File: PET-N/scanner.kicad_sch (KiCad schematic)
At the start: 14 parts, among them J4 AVR-ISP-6, U2 ATmega32A-A, U3 74HCT85, U4 74LS174, U6 74LS174, U7 74LS145, Y1 ASE-xxxMHz

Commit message: almost done routing; last checks still open
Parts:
- added C30: 100n, Capacitor_SMD:C_0805_2012Metric_Pad1.18x1.45mm_HandSolder, symbol Device:C
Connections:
- net GND: now also C30.1
- net VCC: now also C30.2
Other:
- note added: "(C) 2020,2021 Steve J. Gray (C) 2025 André Fachat"
- note added: "CBM-KEYB-PETN-3.0-20251005"
- note added: "This AtMega translates keyboard maps - S0-S1 inputs are on port bits PB0-3, on a port not written to. Reason is they can be read and converted into a table index using ANDI #15 - PB4 could in theory be used to extend the keyboard mapping table - PD2 is falling edge triggered interrupt, fed from the comparison between the S0-3 inputs and their delayed version. - U6 and U4 delay by at least two syt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"
- note removed: "This AtMega translates keyboard maps - S0-S1 inputs are on port bits PB0-3, on a port not written to. Reason is they can be read and converted into a table index using ANDI #15 - PB4 could in theory be used to extend the keyboard mapping table, as fed from PD3. - PD2 is falling edge triggered interrupt, fed from the comparison between the S0-3 inputs and their delayed version. - U6 and U4 delay b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"
- moved on the sheet: C12
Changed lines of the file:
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@@
 	(generator_version "9.0")
 	(paper "A4")
-	(text "This AtMega translates keyboard maps\n- S0-S1 inputs are on port bits PB0-3, on a port\n  not written to. Reason is they can be read and\n  converted into a table index using ANDI #15\n- PB4 could in theory be used to extend the keyboard\n  mapping table, as fed from PD3.\n- PD2 is falling edge triggered interrupt, fed from the\n  comparison between the S0-3 inputs and their delayed\n  version. \n- U6 and U4 delay by at least two sytem clocks cycles, to \n  ensure an interrupt is detected."
+	(text "CBM-KEYB-PETN-3.0-20251005"
 		(exclude_from_sim no)
-		(at 20.574 176.911 0)
+		(at 231.14 172.212 0)
 		(effects
 			(font
-				(size 2 2)
+				(size 4 4)
+				(thickness 0.9)
+				(bold yes)
+			)
+		)
+	)
+	(text "This AtMega translates keyboard maps\n- S0-S1 inputs are on port bits PB0-3, on a port\n  not written to. Reason is they can be read and\n  converted into a table index using ANDI #15\n- PB4 could in theory be used to extend the keyboard\n  mapping table\n- PD2 is falling edge triggered interrupt, fed from the\n  comparison between the S0-3 inputs and their delayed\n  version. \n- U6 and U4 delay by at least two sytem clocks cycles, to \n  ensure an interrupt is detected."
+		(exclude_from_sim no)
+		(at 22.352 173.736 0)
+		(effects
+			(font
+				(size 2.3 2.3)
 			)
 			(justify left)
 		)
 	)
+	(text "(C) 2020,2021 Steve J. Gray\n(C) 2025 André Fachat"
+		(exclude_from_sim no)
+		(at 249.936 181.102 0)
+		(effects
+			(font
+				(size 2.54 2.54)
+				(thickness 0.508)
+				(bold yes)
+			)
+		)
+	)
 	(junction
 		(at 259.08 23.495)
@@
 	)
 	(junction
+		(at 269.875 23.495)
+		(diameter 0)
+		(color 0 0 0 0)
+	)
+	(junction
 		(at 156.21 20.955)
 		(diameter 0)
@@
 	)
 	(junction
+		(at 269.875 36.195)
+		(diameter 0)
+		(color 0 0 0 0)
+	)
+	(junction
 		(at 43.18 26.035)
 		(diameter 0)
@@
 	(wire
 		(pts
-			(xy 270.51 36.195) (xy 259.08 36.195)
-		)
-		(stroke
-			(width 0)
-			(type default)
-		)
-	)
-	(wire
-		(pts
 			(xy 234.95 23.495) (xy 234.95 26.035)
 		)
@@
 	(wire
 		(pts
-			(xy 259.08 23.495) (xy 270.51 23.495)
+			(xy 259.08 23.495) (xy 269.875 23.495)
 		)
 		(stroke
@@
 	(wire
 		(pts
+			(xy 280.67 44.45) (xy 280.67 23.495)
+		)
+		(stroke
+			(width 0)
+			(type default)
+		)
+	)
+	(wire
+		(pts
 			(xy 151.13 125.095) (xy 140.97 125.095)
 		)
@@
 	(wire
 		(pts
+			(xy 269.875 23.495) (xy 280.67 23.495)
+		)
+		(stroke
+			(width 0)
+			(type default)
+		)
+	)
+	(wire
+		(pts
 			(xy 31.75 130.175) (xy 31.75 135.255)
 		)
@@
 	(wire
 		(pts
+			(xy 269.875 44.45) (xy 271.145 44.45)
+		)
+		(stroke
+			(width 0)
+			(type default)
+		)
+	)
+	(wire
+		(pts
 			(xy 247.65 36.195) (xy 234.95 36.195)
 		)
@@
 	(wire
 		(pts
-			(xy 270.51 26.035) (xy 270.51 23.495)
+			(xy 269.875 26.035) (xy 269.875 23.495)
 		)
 		(stroke
@@
 	(wire
 		(pts
+			(xy 269.875 36.195) (xy 259.08 36.195)
+		)
+		(stroke
+			(width 0)
+			(type default)
+		)
+	)
+	(wire
+		(pts
 			(xy 248.92 45.085) (xy 246.38 45.085)
 		)
@@
 	(wire
 		(pts
-			(xy 270.51 33.655) (xy 270.51 36.195)
+			(xy 269.875 33.655) (xy 269.875 36.195)
 		)
 		(stroke
@@
 	(wire
 		(pts
+			(xy 278.765 44.45) (xy 280.67 44.45)
+		)
+		(stroke
+			(width 0)
+			(type default)
+		)
+	)
+	(wire
+		(pts
 			(xy 44.45 23.495) (xy 154.94 23.495)
 		)
@@
 	(wire
 		(pts
+			(xy 269.875 36.195) (xy 269.875 44.45)
+		)
+		(stroke
+			(width 0)
+			(type default)
+		)
+	)
+	(wire
+		(pts
 			(xy 234.95 33.655) (xy 234.95 36.195)
 		)
@@
 	(symbol
 		(lib_id "Device:C")
-		(at 270.51 29.845 0)
+		(at 269.875 29.845 0)
 		(unit 1)
 		(exclude_from_sim no)
@@
 		(fields_autoplaced yes)
 		(property "Reference" "C12"
-			(at 274.32 28.5749 0)
+			(at 273.685 28.5749 0)
 			(effects
 				(font
@@
 		)
 		(property "Value" "100n"
-			(at 274.32 31.1149 0)
+			(at 273.685 31.1149 0)
 			(effects
 				(font
@@
 		)
 		(property "Footprint" "Capacitor_SMD:C_0805_2012Metric_Pad1.18x1.45mm_HandSolder"
-			(at 271.4752 33.655 0)
+			(at 270.8402 33.655 0)
 			(effects
 				(font
@@
 		)
 		(property "Datasheet" "~"
-			(at 270.51 29.845 0)
+			(at 269.875 29.845 0)
 			(effects
 				(font
@@
 		)
 		(property "Description" "Unpolarized capacitor"
-			(at 270.51 29.845 0)
+			(at 269.875 29.845 0)
 			(effects
 				(font
@@
 		)
 		(property "LCSC" "C14663"
-			(at 274.32 28.5749 0)
+			(at 273.685 28.5749 0)
 			(effects
 				(font
@@
 					(unit 1)
 				)
+			)
+		)
+	)
+	(symbol
+		(lib_id "Device:C")
+		(at 274.955 44.45 90)
+		(unit 1)
+		(exclude_from_sim no)
+		(in_bom yes)
+		(on_board yes)
+		(dnp no)
+		(fields_autoplaced yes)
+		(property "Reference" "C30"
+			(at 274.955 36.83 90)
+			(effects
+				(font
+					(size 1.27 1.27)
+				)
+			)
+		)
+		(property "Value" "100n"
+			(at 274.955 39.37 90)
+			(effects
+				(font
+					(size 1.27 1.27)
+				)
+			)
+		)
+		(property "Footprint" "Capacitor_SMD:C_0805_2012Metric_Pad1.18x1.45mm_HandSolder"
+			(at 278.765 43.4848 0)
+			(effects
+				(font
+					(size 1.27 1.27)
+				)
+				(hide yes)
+			)
+		)
+		(property "Datasheet" "~"
+			(at 274.955 44.45 0)
+			(effects
+				(font
+					(size 1.27 1.27)
+				)
+				(hide yes)
+			)
+		)
+		(property "Description" "Unpolarized capacitor"
+			(at 274.955 44.45 0)
+			(effects
+				(font
+					(size 1.27 1.27)
+				)
+				(hide yes)
+			)
+		)
+		(property "LCSC" "C14663"
+			(at 273.6849 40.64 0)
+			(effects
+				(font
+					(size 1.27 1.27)
+				)
+				(hide yes)
+			)
+		)
+		(pin "2"
+		)
+		(pin "1"
+		)
+		(instances
+			(project "petkn"
+				(path "/a0727808-af70-4056-b2ee-ab828c2acfbd/517ec251-9cce-431a-9802-232702808e0f"
+					(reference "C30")
+					(unit 1)
+				)

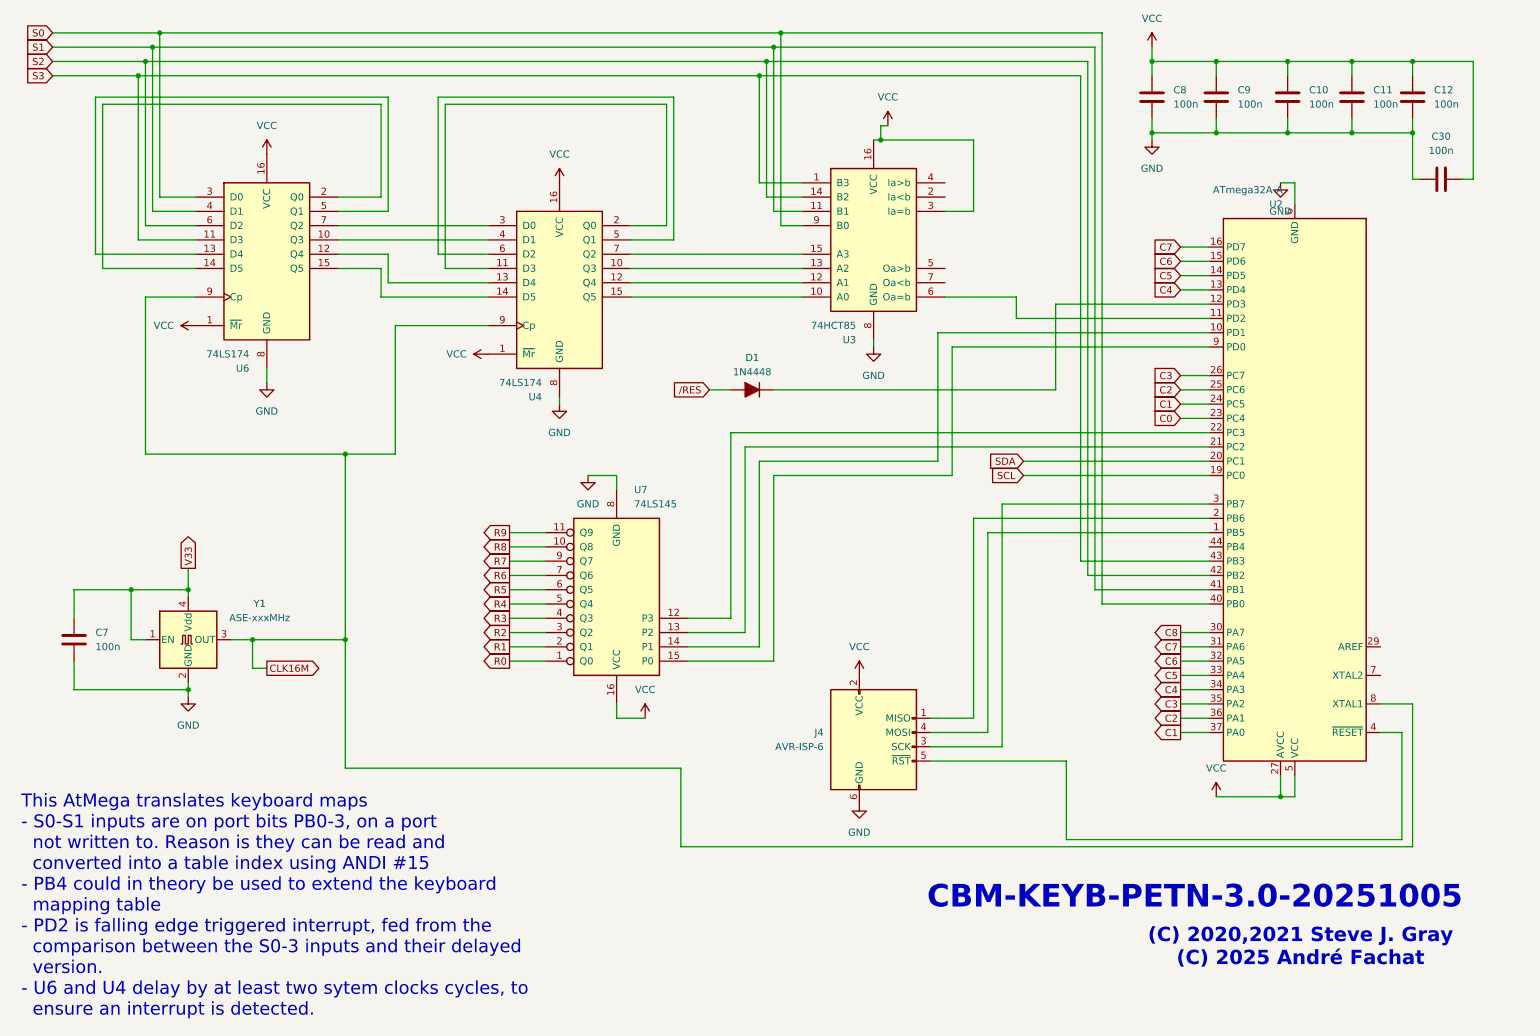
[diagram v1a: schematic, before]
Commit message: fix Cn vs CCn bug, add proper joystick in schem; routing still to fix
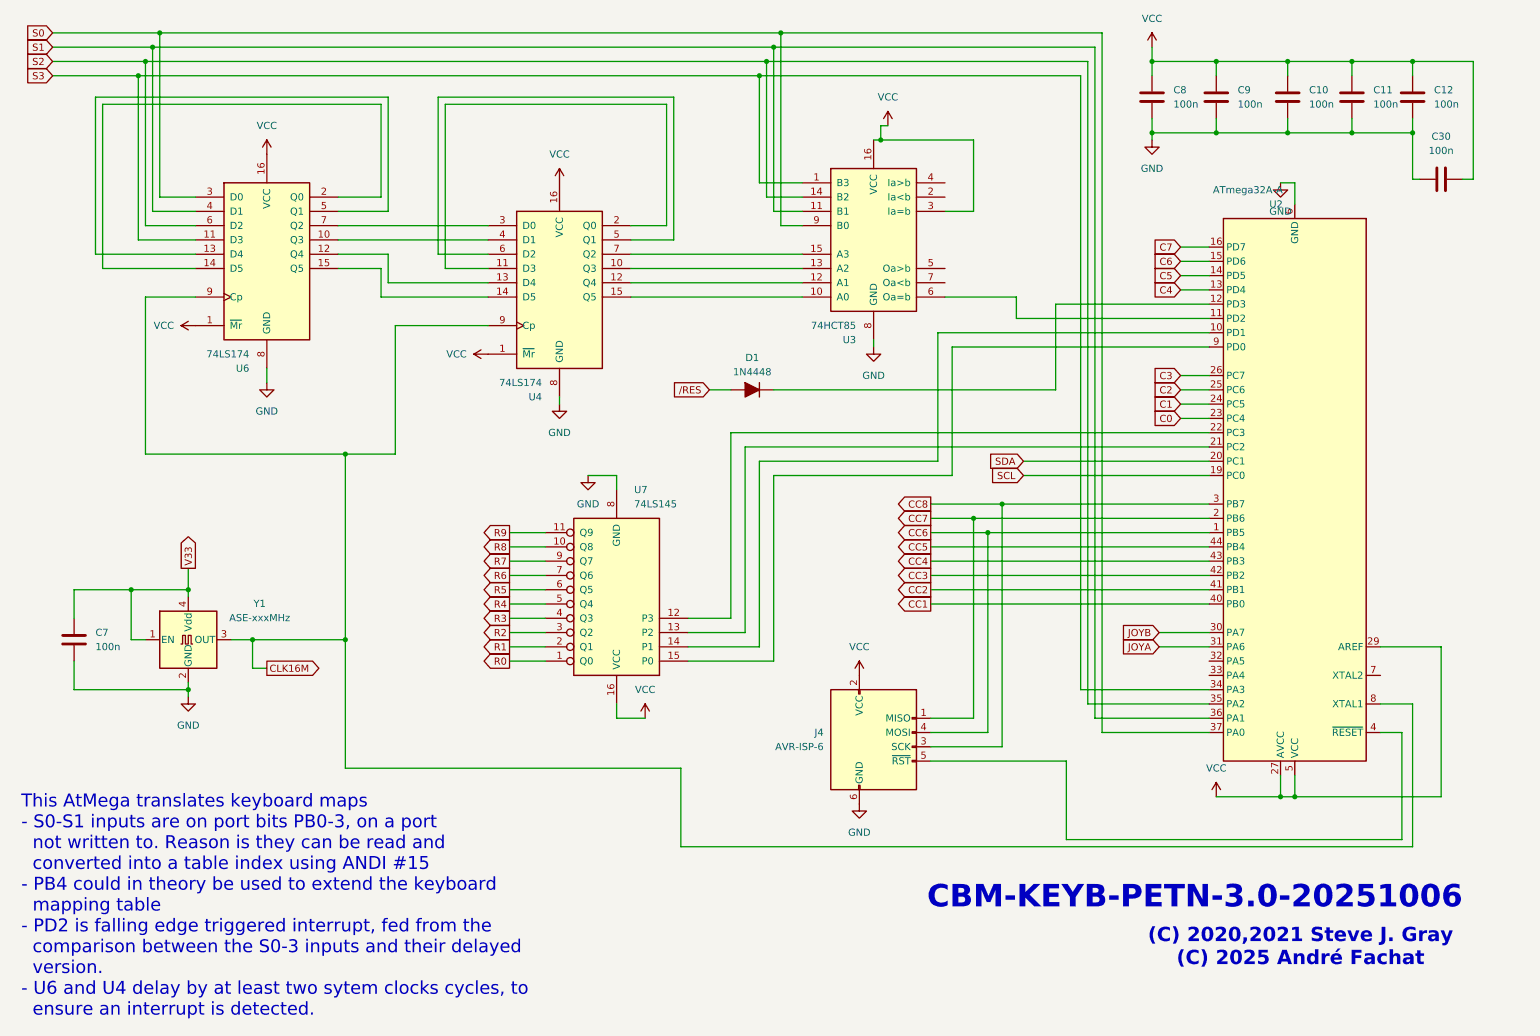
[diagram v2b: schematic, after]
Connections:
- net C1: no longer U2.37 (PA0)
- net C2: no longer U2.36 (PA1)
- net C3: no longer U2.35 (PA2)
- net C4: no longer U2.34 (PA3)
- net C5: no longer U2.33 (PA4)
- net C6: no longer U2.32 (PA5)
- net C7: no longer U2.31 (PA6)
- net S0: now also U2.37 (PA0); no longer U2.40 (PB0)
- net S1: now also U2.36 (PA1); no longer U2.41 (PB1)
- net S2: now also U2.35 (PA2); no longer U2.42 (PB2)
- net S3: now also U2.34 (PA3); no longer U2.43 (PB3)
- net VCC: now also U2.29 (AREF)
- net CC7: now reaches J4.1 (MISO), U2.2 (PB6)
- net CC8: now reaches J4.3 (SCK), U2.3 (PB7)
- net CC6: now reaches J4.4 (MOSI), U2.1 (PB5)
- net CC5: now reaches U2.44 (PB4)
- net C8 renamed JOYB
- new net CC1: U2.40 (PB0)
- new net CC2: U2.41 (PB1)
- new net CC3: U2.42 (PB2)
- new net CC4: U2.43 (PB3)
- new net JOYA: U2.31 (PA6)
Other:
- note added: "CBM-KEYB-PETN-3.0-20251006"
- note removed: "CBM-KEYB-PETN-3.0-20251005"

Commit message: hopefully final schem and layout for 3.0A
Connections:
- net C0 is gone; now on net C1: U2.23 (PC4)
- net C1: no longer U2.24 (PC5)
- net C2: now also U2.24 (PC5); no longer U2.25 (PC6)
- net C3: now also U2.25 (PC6); no longer U2.26 (PC7)
- net C4: now also U2.26 (PC7); no longer U2.13 (PD4)
- net C5: now also U2.13 (PD4); no longer U2.14 (PD5)
- net C6: now also U2.14 (PD5); no longer U2.15 (PD6)
- net C7: now also U2.15 (PD6); no longer U2.16 (PD7)
- new net C8: U2.16 (PD7)
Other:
- note added: "CBM-KEYB-PETN-3.0A-20251011"
- note added: "This AtMega translates keyboard maps - S0-S1 inputs are on port bits PA0-3, on a port not written to. Reason is they can be read and converted into a table index using ANDI #15 - PA4/5 could in theory be used to extend the keyboard mapping table - PD2 is falling edge triggered interrupt, fed from the comparison between the S0-3 inputs and their delayed version. - U6 and U4 delay by at least two s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"
- note removed: "CBM-KEYB-PETN-3.0-20251006"
- note removed: "This AtMega translates keyboard maps - S0-S1 inputs are on port bits PB0-3, on a port not written to. Reason is they can be read and converted into a table index using ANDI #15 - PB4 could in theory be used to extend the keyboard mapping table - PD2 is falling edge triggered interrupt, fed from the comparison between the S0-3 inputs and their delayed version. - U6 and U4 delay by at least two syt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"
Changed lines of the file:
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@@
 	(generator_version "9.0")
 	(paper "A4")
-	(text "CBM-KEYB-PETN-3.0-20251006"
+	(text "CBM-KEYB-PETN-3.0A-20251011"
 		(exclude_from_sim no)
 		(at 231.14 172.212 0)
@@
 		)
 	)
-	(text "This AtMega translates keyboard maps\n- S0-S1 inputs are on port bits PB0-3, on a port\n  not written to. Reason is they can be read and\n  converted into a table index using ANDI #15\n- PB4 could in theory be used to extend the keyboard\n  mapping table\n- PD2 is falling edge triggered interrupt, fed from the\n  comparison between the S0-3 inputs and their delayed\n  version. \n- U6 and U4 delay by at least two sytem clocks cycles, to \n  ensure an interrupt is detected."
+	(text "This AtMega translates keyboard maps\n- S0-S1 inputs are on port bits PA0-3, on a port\n  not written to. Reason is they can be read and\n  converted into a table index using ANDI #15\n- PA4/5 could in theory be used to extend the keyboard\n  mapping table\n- PD2 is falling edge triggered interrupt, fed from the\n  comparison between the S0-3 inputs and their delayed\n  version. \n- U6 and U4 delay by at least two sytem clocks cycles, to \n  ensure an interrupt is detected."
 		(exclude_from_sim no)
 		(at 22.352 173.736 0)
@@
 		)
 	)
-	(global_label "C5"
+	(global_label "C6"
 		(shape input)
 		(at 228.6 61.595 180)
@@
 		)
 	)
-	(global_label "C4"
+	(global_label "C5"
 		(shape input)
 		(at 228.6 64.135 180)
@@
 		)
 	)
-	(global_label "C0"
+	(global_label "C1"
 		(shape input)
 		(at 228.6 86.995 180)
@@
 		)
 	)
-	(global_label "C7"
+	(global_label "C8"
 		(shape input)
 		(at 228.6 56.515 180)
@@
 		)
 	)
-	(global_label "C6"
+	(global_label "C7"
 		(shape input)
 		(at 228.6 59.055 180)
@@
 		)
 	)
-	(global_label "C3"
+	(global_label "C4"
 		(shape input)
 		(at 228.6 79.375 180)
@@
 		)
 	)
-	(global_label "C2"
+	(global_label "C3"
 		(shape input)
 		(at 228.6 81.915 180)
@@
 		)
 	)
-	(global_label "C1"
+	(global_label "C2"
 		(shape input)
 		(at 228.6 84.455 180)

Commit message: small layout updates, jlcpcb production files
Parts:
- D1: footprint Diode_SMD:D_0603_1608Metric -> Diode_SMD:D_SOD-323_HandSoldering
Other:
- note added: "CBM-KEYB-PETN-3.0A-20251012"
- note removed: "CBM-KEYB-PETN-3.0A-20251011"
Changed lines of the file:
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@@
 	(generator_version "9.0")
 	(paper "A4")
-	(text "CBM-KEYB-PETN-3.0A-20251011"
+	(text "CBM-KEYB-PETN-3.0A-20251012"
 		(exclude_from_sim no)
 		(at 231.14 172.212 0)
@@
 			)
 		)
-		(property "Footprint" "Diode_SMD:D_0603_1608Metric"
+		(property "Footprint" "Diode_SMD:D_SOD-323_HandSoldering"
 			(at 152.4 81.915 0)
 			(effects

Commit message: as sent to production
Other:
- note added: "CBM-KEYB-PETN-3.0A-20251014"
- note removed: "CBM-KEYB-PETN-3.0A-20251012"
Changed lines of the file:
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@@
 	(generator_version "9.0")
 	(paper "A4")
-	(text "CBM-KEYB-PETN-3.0A-20251012"
+	(text "CBM-KEYB-PETN-3.0A-20251014"
 		(exclude_from_sim no)
 		(at 231.14 172.212 0)

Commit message: fix the two 3.0A issues (temporarily)
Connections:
- net R0 renamed R10
- net V33 renamed VCC33
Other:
- note added: "CBM-KEYB-PETN-3.0B-20251102"
- note removed: "CBM-KEYB-PETN-3.0A-20251014"
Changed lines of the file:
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@@
 	(generator_version "9.0")
 	(paper "A4")
-	(text "CBM-KEYB-PETN-3.0A-20251014"
+	(text "CBM-KEYB-PETN-3.0B-20251102"
 		(exclude_from_sim no)
 		(at 231.14 172.212 0)
@@
 		)
 	)
+	(global_label "R10"
+		(shape output)
+		(at 109.22 130.175 180)
+		(fields_autoplaced yes)
+		(effects
+			(font
+				(size 1.27 1.27)
+			)
+			(justify right)
+		)
+		(property "Intersheetrefs" "${INTERSHEET_REFS}"
+			(at 103.2 130.175 0)
+			(effects
+				(font
+					(size 1.27 1.27)
+				)
+				(justify right)
+				(hide yes)
+			)
+		)
+	)
 	(global_label "R9"
 		(shape output)
@@
 		)
 	)
-	(global_label "V33"
-		(shape output)
-		(at 52.07 113.665 90)
-		(fields_autoplaced yes)
-		(effects
-			(font
-				(size 1.27 1.27)
-			)
-			(justify left)
-		)
-		(property "Intersheetrefs" "${INTERSHEET_REFS}"
-			(at 52.07 107.1722 90)
-			(effects
-				(font
-					(size 1.27 1.27)
-				)
-				(justify left)
-				(hide yes)
-			)
-		)
-	)
 	(global_label "R4"
 		(shape output)
@@
 		)
 	)
+	(global_label "VCC33"
+		(shape input)
+		(at 52.07 113.665 90)
+		(fields_autoplaced yes)
+		(effects
+			(font
+				(size 1.27 1.27)
+			)
+			(justify left)
+		)
+		(property "Intersheetrefs" "${INTERSHEET_REFS}"
+			(at 52.07 105.2864 90)
+			(effects
+				(font
+					(size 1.27 1.27)
+				)
+				(justify left)
+				(hide yes)
+			)
+		)
+	)
 	(global_label "R1"
 		(shape output)
@@
 				(hide yes)
 			)
-		)
-	)
-	(global_label "R0"
-		(shape output)
-		(at 109.22 130.175 180)
-		(fields_autoplaced yes)
-		(effects
-			(font
-				(size 1.27 1.27)
-			)
-			(justify right)
-		)
-		(property "Intersheetrefs" "${INTERSHEET_REFS}"
-			(at 104.4095 130.175 0)
-			(effects
-				(font
-					(size 1.27 1.27)
-				)
-				(justify right)
-				(hide yes)
-			)

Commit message: first run on r3.1
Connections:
- net R1: now also U7.1 (Q0); no longer U7.2 (Q1)
- net R10: now also U7.11 (Q9); no longer U7.1 (Q0)
- net R2: now also U7.2 (Q1); no longer U7.3 (Q2)
- net R3: now also U7.3 (Q2); no longer U7.4 (Q3)
- net R4: now also U7.4 (Q3); no longer U7.5 (Q4)
- net R5: now also U7.5 (Q4); no longer U7.6 (Q5)
- net R6: now also U7.6 (Q5); no longer U7.7 (Q6)
- net R7: now also U7.7 (Q6); no longer U7.9 (Q7)
- net R8: now also U7.9 (Q7); no longer U7.10 (Q8)
- net R9: now also U7.10 (Q8); no longer U7.11 (Q9)
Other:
- note added: "(C) 2020, 2021 Steve J. Gray (C) 2025, 2026 André Fachat"
- note added: "CBM-KEYB-PETN-3.1A-20260130"
- note removed: "(C) 2020,2021 Steve J. Gray (C) 2025 André Fachat"
- note removed: "CBM-KEYB-PETN-3.0B-20251102"
- moved on the sheet: U7
